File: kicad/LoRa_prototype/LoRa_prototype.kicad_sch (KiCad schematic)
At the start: 1 part, among them U1 STM32WL55JCIx

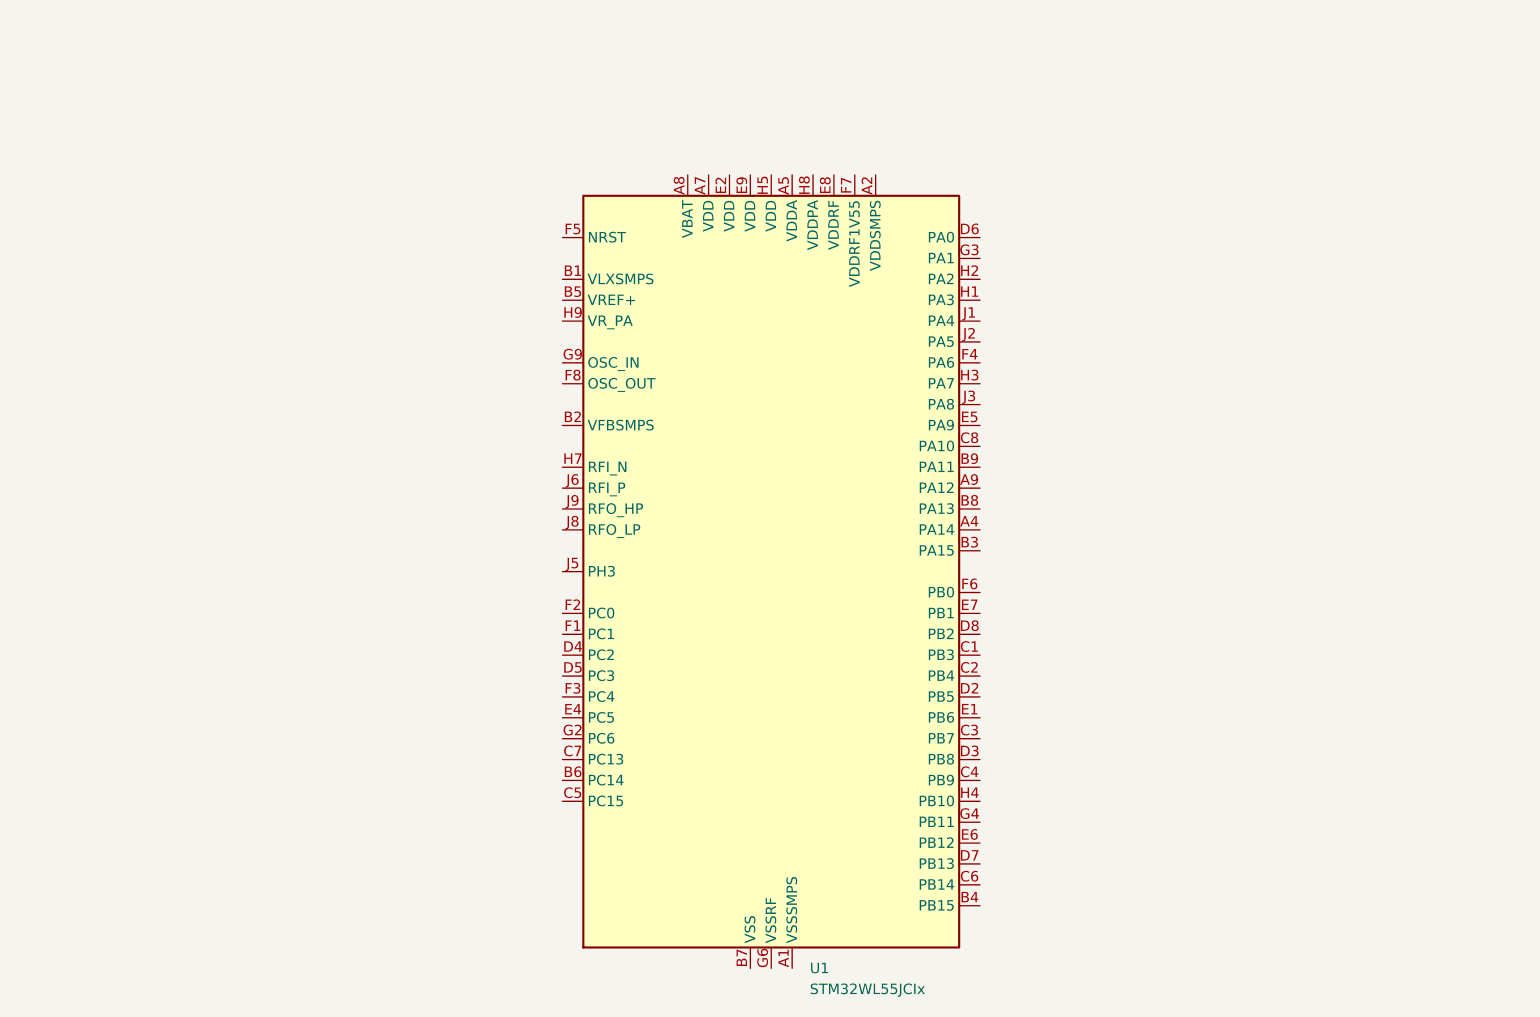
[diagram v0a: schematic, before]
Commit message: Implement power decoupling in schematic
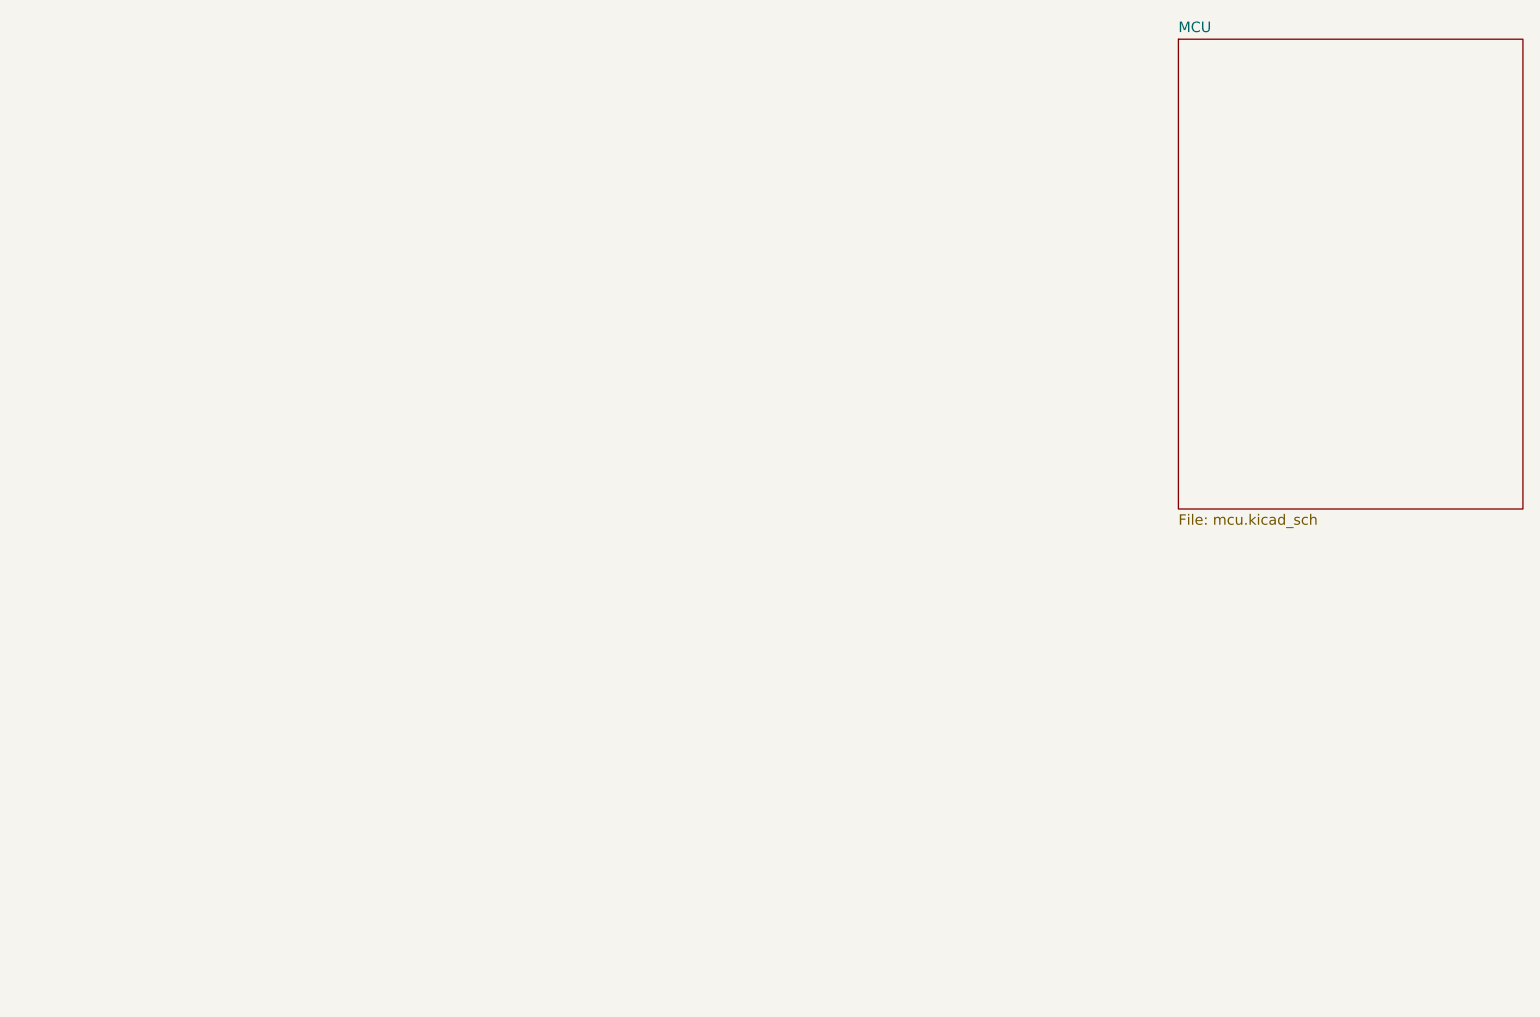
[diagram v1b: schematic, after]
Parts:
- removed U1: STM32WL55JCIx, Package_BGA:ST_UFBGA-73_5x5mm_Layout9x9_P0.5mm, symbol MCU_ST_STM32WL:STM32WL55JCIx
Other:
- added sheet MCU (mcu.kicad_sch)
- company: (none) -> DesCap GmbH
- title: (none) -> LoRa hardware prototype
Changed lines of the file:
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@@
 	(generator_version "9.0")
 	(paper "A4")
-	(symbol
-		(lib_id "MCU_ST_STM32WL:STM32WL55JCIx")
-		(at 115.57 97.79 0)
-		(unit 1)
+	(title_block
+		(title "LoRa hardware prototype")
+		(date "2026-04-08")
+		(rev "A")
+		(company "DesCap GmbH")
+	)
+	(sheet
+		(at 165.1 33.02)
+		(size 41.91 57.15)
 		(exclude_from_sim no)
 		(in_bom yes)
@@
 		(dnp no)
 		(fields_autoplaced yes)
-		(property "Reference" "U1"
-			(at 120.2533 146.05 0)
+		(stroke
+			(width 0.1524)
+			(type solid)
+		)
+		(fill
+			(color 0 0 0 0.0000)
+		)
+		(property "Sheetname" "MCU"
+			(at 165.1 32.3084 0)
 			(effects
 				(font
 					(size 1.27 1.27)
 				)
-				(justify left)
+				(justify left bottom)
 			)
 		)
-		(property "Value" "STM32WL55JCIx"
-			(at 120.2533 148.59 0)
+		(property "Sheetfile" "mcu.kicad_sch"
+			(at 165.1 90.7546 0)
 			(effects
 				(font
 					(size 1.27 1.27)
 				)
-				(justify left)
+				(justify left top)
 			)
 		)
-		(property "Footprint" "Package_BGA:ST_UFBGA-73_5x5mm_Layout9x9_P0.5mm"
-			(at 92.71 143.51 0)
-			(effects
-				(font
-					(size 1.27 1.27)
-				)
-				(justify right)
-				(hide yes)
-			)
-		)
-		(property "Datasheet" "https://www.st.com/resource/en/datasheet/stm32wl55jc.pdf"
-			(at 115.57 97.79 0)
-			(effects
-				(font
-					(size 1.27 1.27)
-				)
-				(hide yes)
-			)
-		)
-		(property "Description" "STMicroelectronics Arm Cortex-M4 MCU, 256KB flash, 64KB RAM, 48 MHz, 1.8-3.6V, 43 GPIO, UFBGA73"
-			(at 115.57 97.79 0)
-			(effects
-				(font
-					(size 1.27 1.27)
-				)
-				(hide yes)
-			)
-		)
-		(pin "F8"
-		)
-		(pin "A8"
-		)
-		(pin "E9"
-		)
-		(pin "B2"
-		)
-		(pin "D5"
-		)
-		(pin "G5"
-		)
-		(pin "H9"
-		)
-		(pin "C5"
-		)
-		(pin "F1"
-		)
-		(pin "E2"
-		)
-		(pin "H7"
-		)
-		(pin "B1"
-		)
-		(pin "G9"
-		)
-		(pin "J9"
-		)
-		(pin "F2"
-		)
-		(pin "D4"
-		)
-		(pin "E4"
-		)
-		(pin "C7"
-		)
-		(pin "F5"
-		)
-		(pin "J6"
-		)
-		(pin "B5"
-		)
-		(pin "F3"
-		)
-		(pin "B6"
-		)
-		(pin "G2"
-		)
-		(pin "J8"
-		)
-		(pin "J5"
-		)
-		(pin "A7"
-		)
-		(pin "B7"
-		)
-		(pin "D9"
-		)
-		(pin "E3"
-		)
-		(pin "A1"
-		)
-		(pin "A5"
-		)
-		(pin "F4"
-		)
-		(pin "H6"
-		)
-		(pin "G6"
-		)
-		(pin "E7"
-		)
-		(pin "C1"
-		)
-		(pin "H8"
-		)
-		(pin "F6"
-		)
-		(pin "G7"
-		)
-		(pin "E8"
-		)
-		(pin "A2"
-		)
-		(pin "G8"
-		)
-		(pin "H1"
-		)
-		(pin "J2"
-		)
-		(pin "B9"
-		)
-		(pin "D6"
-		)
-		(pin "J1"
-		)
-		(pin "H3"
-		)
-		(pin "A9"
-		)
-		(pin "F7"
-		)
-		(pin "E5"
-		)
-		(pin "B8"
-		)
-		(pin "C8"
-		)
-		(pin "H5"
-		)
-		(pin "H2"
-		)
-		(pin "G3"
-		)
-		(pin "B3"
-		)
-		(pin "J3"
-		)
-		(pin "A4"
-		)
-		(pin "D8"
-		)
-		(pin "C2"
-		)
-		(pin "D2"
-		)
-		(pin "E1"
-		)
-		(pin "C3"
-		)
-		(pin "G4"
-		)
-		(pin "D7"
-		)
-		(pin "C6"
-		)
-		(pin "B4"
-		)
-		(pin "E6"
-		)
-		(pin "D3"
-		)
-		(pin "H4"
-		)
-		(pin "C4"
-		)
 		(instances
-			(project ""
+			(project "LoRa_prototype"
 				(path "/9fad4700-f514-47ad-821a-b4076ecc08de"
-					(reference "U1")
-					(unit 1)
+					(page "2")
 				)
 			)

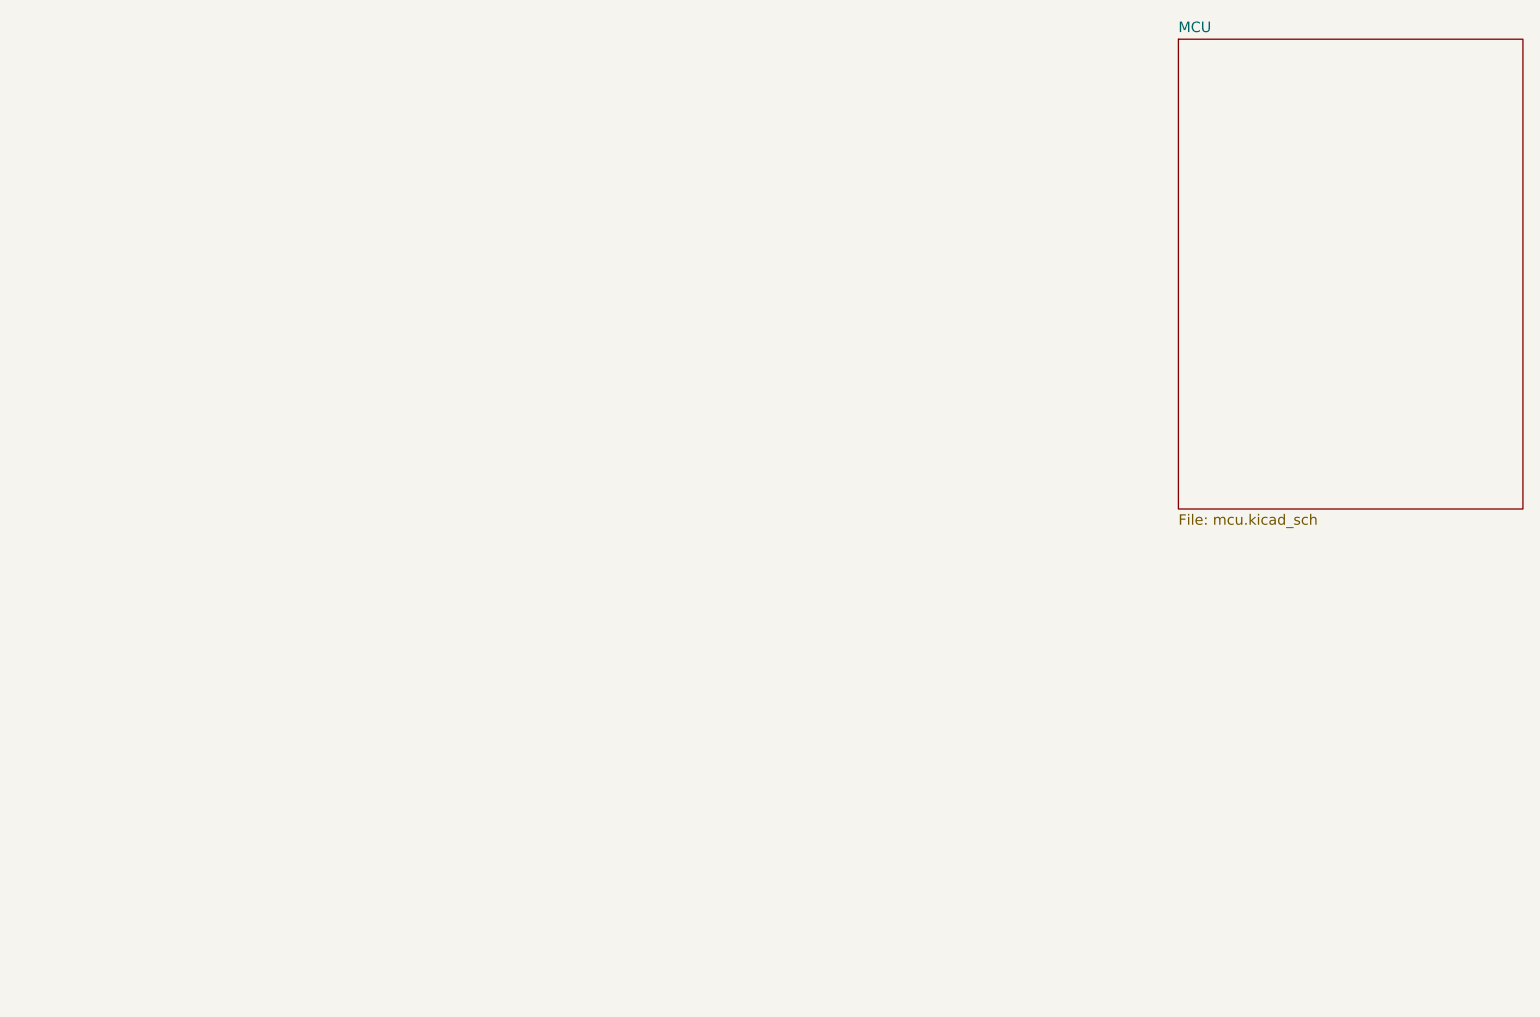
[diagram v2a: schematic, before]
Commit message: Reorganized schematic
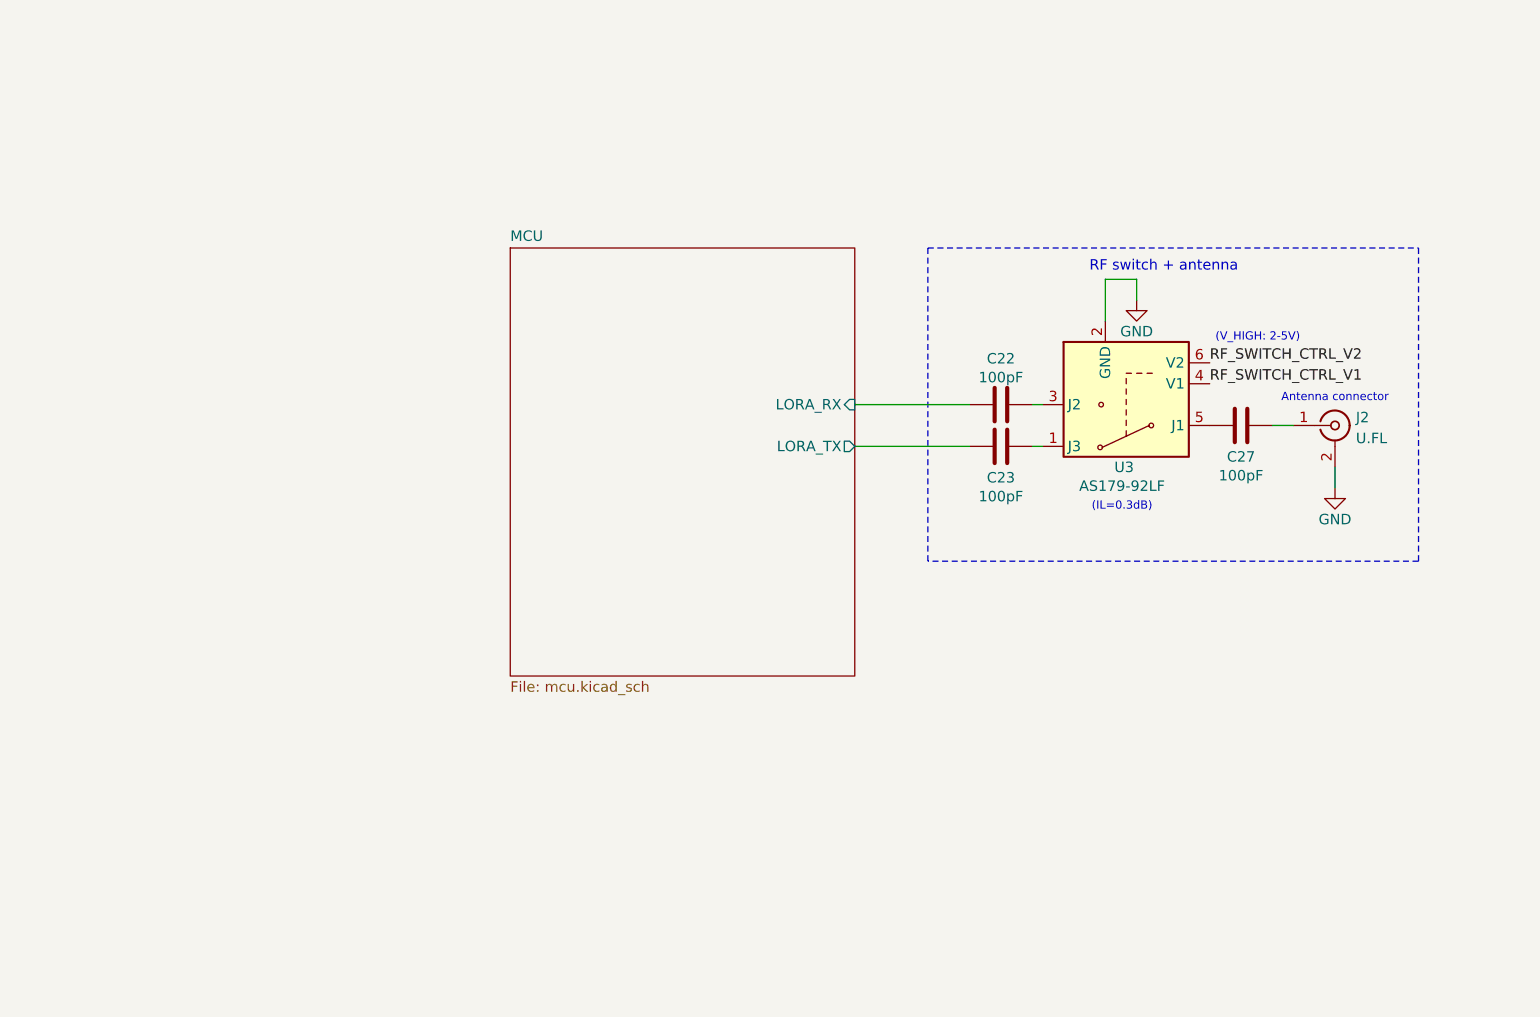
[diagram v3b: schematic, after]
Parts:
- added C22, C23, C27: 100pF, symbol Device:C
- added J2: U.FL, PCM_JLCPCB:IPEX-SMD_BWIPX-1-001E, symbol PCM_JLCPCB-Extended:RF, Connector, U.FL
- added U3: AS179-92LF, Package_TO_SOT_SMD:SOT-363_SC-70-6, symbol RF_Switch:AS179-92LF
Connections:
- new net: C23.2, U3.1 (J3)
- new net: C22.2, U3.3 (J2)
- new net: C27.1, U3.5 (J1)
- new net: C27.2, J2.1 (In)
- new net GND: J2.2 (Ext), U3.2 (GND)
- new net MCU/LORA_RX: C22.1
- new net MCU/LORA_TX: C23.1
- new net RF_SWITCH_CTRL_V1: U3.4 (V1)
- new net RF_SWITCH_CTRL_V2: U3.6 (V2)
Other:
- sheet MCU ports: added LORA_RX, LORA_TX; removed none
- note added: "(IL=0.3dB)"
- note added: "(V_HIGH: 2-5V)"
- note added: "Antenna connector"
- note added: "RF switch + antenna"

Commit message: Done doing MCU schematic (Milestone)
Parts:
- added J1: Conn_ST_STDC14, Connector_PinHeader_1.27mm:PinHeader_2x07_P1.27mm_Vertical, symbol Connector:Conn_ST_STDC14
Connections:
- new net: J1.5 (GND), J1.7 (GND)
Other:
- moved on the sheet: C22, C23, C27, J2, U3
